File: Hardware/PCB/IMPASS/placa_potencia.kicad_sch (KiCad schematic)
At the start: 14 parts, among them J11 SOLENOIDES, J2 POWER, J22 VM, J23 EJE1, J24 EJE2, J25 EJE3, J26 SOLENOIDES, J27 PUENTE H, J28 PUENTE H, J29 SENSORES

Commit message: Hardware: update schematic and PCB layout
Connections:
- net Eje1/OUT1_1: no longer J23.2 (Pin_2)
- net Eje1/OUT2_1: no longer J23.4 (Pin_4)
- net Eje2/OUT3_1: no longer J24.2 (Pin_2)
- net Eje2/OUT4_1: no longer J24.4 (Pin_4)
- net Eje3/OUT5_1: no longer J25.4 (Pin_4)
- net Eje3/OUT6_1: no longer J25.2 (Pin_2)
- net Sensores_potencia/SCL: now also J29.8 (Pin_8); no longer J29.7 (Pin_7)
- net Sensores_potencia/SDA: now also J29.7 (Pin_7); no longer J29.8 (Pin_8)
- new net Sensores_potencia/OUT1_2: J23.2 (Pin_2)
- new net Sensores_potencia/OUT2_2: J23.4 (Pin_4)
- new net Sensores_potencia/OUT3_2: J24.2 (Pin_2)
- new net Sensores_potencia/OUT4_2: J24.4 (Pin_4)
- new net Sensores_potencia/OUT5_2: J25.4 (Pin_4)
- new net Sensores_potencia/OUT6_2: J25.2 (Pin_2)
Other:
- sheet Sensores_potencia ports: added IN1_1, IN2_1, IN3_1, IN4_1, IN5_1, IN6_1; removed OUT1_1, OUT2_1, OUT3_1, OUT4_1, OUT5_1, OUT6_1

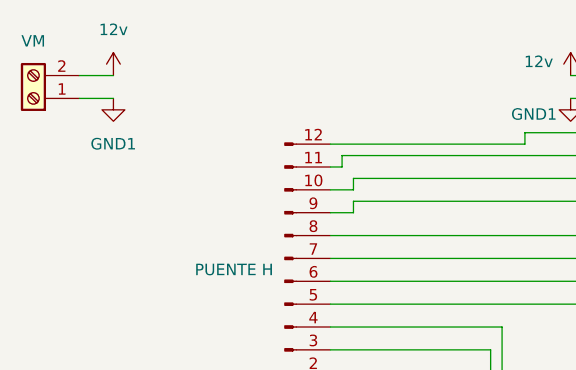
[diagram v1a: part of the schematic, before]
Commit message: Hardware: update schematic and PCB layout 	- Replace the LDOs with buck converters 	- Replace AD5047D with LIS3DH
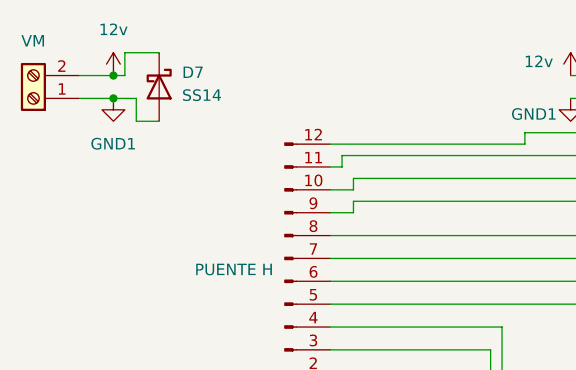
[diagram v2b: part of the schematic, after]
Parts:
- added D7: SS14, Diode_SMD:D_SMA, symbol Diode:SS14
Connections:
- net 12v: now also D7.1 (K)
- net GND1: now also D7.2 (A)
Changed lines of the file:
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@@
 		(comment 2 "Esta es la placa de potencia")
 	)
+	(junction
+		(at 45.72 20.32)
+		(diameter 0)
+		(color 0 0 0 0)
+	)
+	(junction
+		(at 45.72 17.78)
+		(diameter 0)
+		(color 0 0 0 0)
+	)
 	(wire
 		(pts
@@
 	(wire
 		(pts
+			(xy 50.8 15.24) (xy 46.99 15.24)
+		)
+		(stroke
+			(width 0)
+			(type default)
+		)
+	)
+	(wire
+		(pts
 			(xy 148.59 29.21) (xy 152.4 29.21)
 		)
@@
 	(wire
 		(pts
+			(xy 48.26 20.32) (xy 45.72 20.32)
+		)
+		(stroke
+			(width 0)
+			(type default)
+		)
+	)
+	(wire
+		(pts
 			(xy 152.4 68.58) (xy 153.67 68.58)
 		)
@@
 	(wire
 		(pts
+			(xy 46.99 17.78) (xy 45.72 17.78)
+		)
+		(stroke
+			(width 0)
+			(type default)
+		)
+	)
+	(wire
+		(pts
 			(xy 67.31 91.44) (xy 71.12 91.44)
 		)
@@
 	(wire
 		(pts
+			(xy 48.26 22.86) (xy 48.26 20.32)
+		)
+		(stroke
+			(width 0)
+			(type default)
+		)
+	)
+	(wire
+		(pts
 			(xy 151.13 81.28) (xy 151.13 104.14)
 		)
@@
 	(wire
 		(pts
+			(xy 46.99 15.24) (xy 46.99 17.78)
+		)
+		(stroke
+			(width 0)
+			(type default)
+		)
+	)
+	(wire
+		(pts
 			(xy 97.79 92.71) (xy 102.87 92.71)
 		)
@@
 	(wire
 		(pts
+			(xy 50.8 22.86) (xy 48.26 22.86)
+		)
+		(stroke
+			(width 0)
+			(type default)
+		)
+	)
+	(wire
+		(pts
 			(xy 69.85 93.98) (xy 67.31 93.98)
 		)
@@
 					(unit 1)
 				)
+			)
+		)
+	)
+	(symbol
+		(lib_id "Diode:SS14")
+		(at 50.8 19.05 270)
+		(unit 1)
+		(body_style 1)
+		(exclude_from_sim no)
+		(in_bom yes)
+		(on_board yes)
+		(in_pos_files yes)
+		(dnp no)
+		(fields_autoplaced yes)
+		(property "Reference" "D7"
+			(at 53.34 17.4624 90)
+			(show_name no)
+			(do_not_autoplace no)
+			(effects
+				(font
+					(size 1.27 1.27)
+				)
+				(justify left)
+			)
+		)
+		(property "Value" "SS14"
+			(at 53.34 20.0024 90)
+			(show_name no)
+			(do_not_autoplace no)
+			(effects
+				(font
+					(size 1.27 1.27)
+				)
+				(justify left)
+			)
+		)
+		(property "Footprint" "Diode_SMD:D_SMA"
+			(at 46.355 19.05 0)
+			(hide yes)
+			(show_name no)
+			(do_not_autoplace no)
+			(effects
+				(font
+					(size 1.27 1.27)
+				)
+			)
+		)
+		(property "Datasheet" "https://www.vishay.com/docs/88746/ss12.pdf"
+			(at 50.8 19.05 0)
+			(hide yes)
+			(show_name no)
+			(do_not_autoplace no)
+			(effects
+				(font
+					(size 1.27 1.27)
+				)
+			)
+		)
+		(property "Description" "40V 1A Schottky Diode, SMA"
+			(at 50.8 19.05 0)
+			(hide yes)
+			(show_name no)
+			(do_not_autoplace no)
+			(effects
+				(font
+					(size 1.27 1.27)
+				)
+			)
+		)
+		(pin "2"
+		)
+		(pin "1"
+		)
+		(instances
+			(project "IMPASS"
+				(path "/731b3037-3e9a-4423-b2c0-b5bf223d88c2/acd98061-6367-4cb8-aa42-1ec0ef88ad06"
+					(reference "D7")
+					(unit 1)
+				)
